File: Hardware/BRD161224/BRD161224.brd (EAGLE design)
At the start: 100 x 80 mm, 16 parts, among them Q1 DMP2035, Q2 FDV301, Q3 FDV301, Q4 DMP2035, Q5 DMP2035, Q6 DMP2035

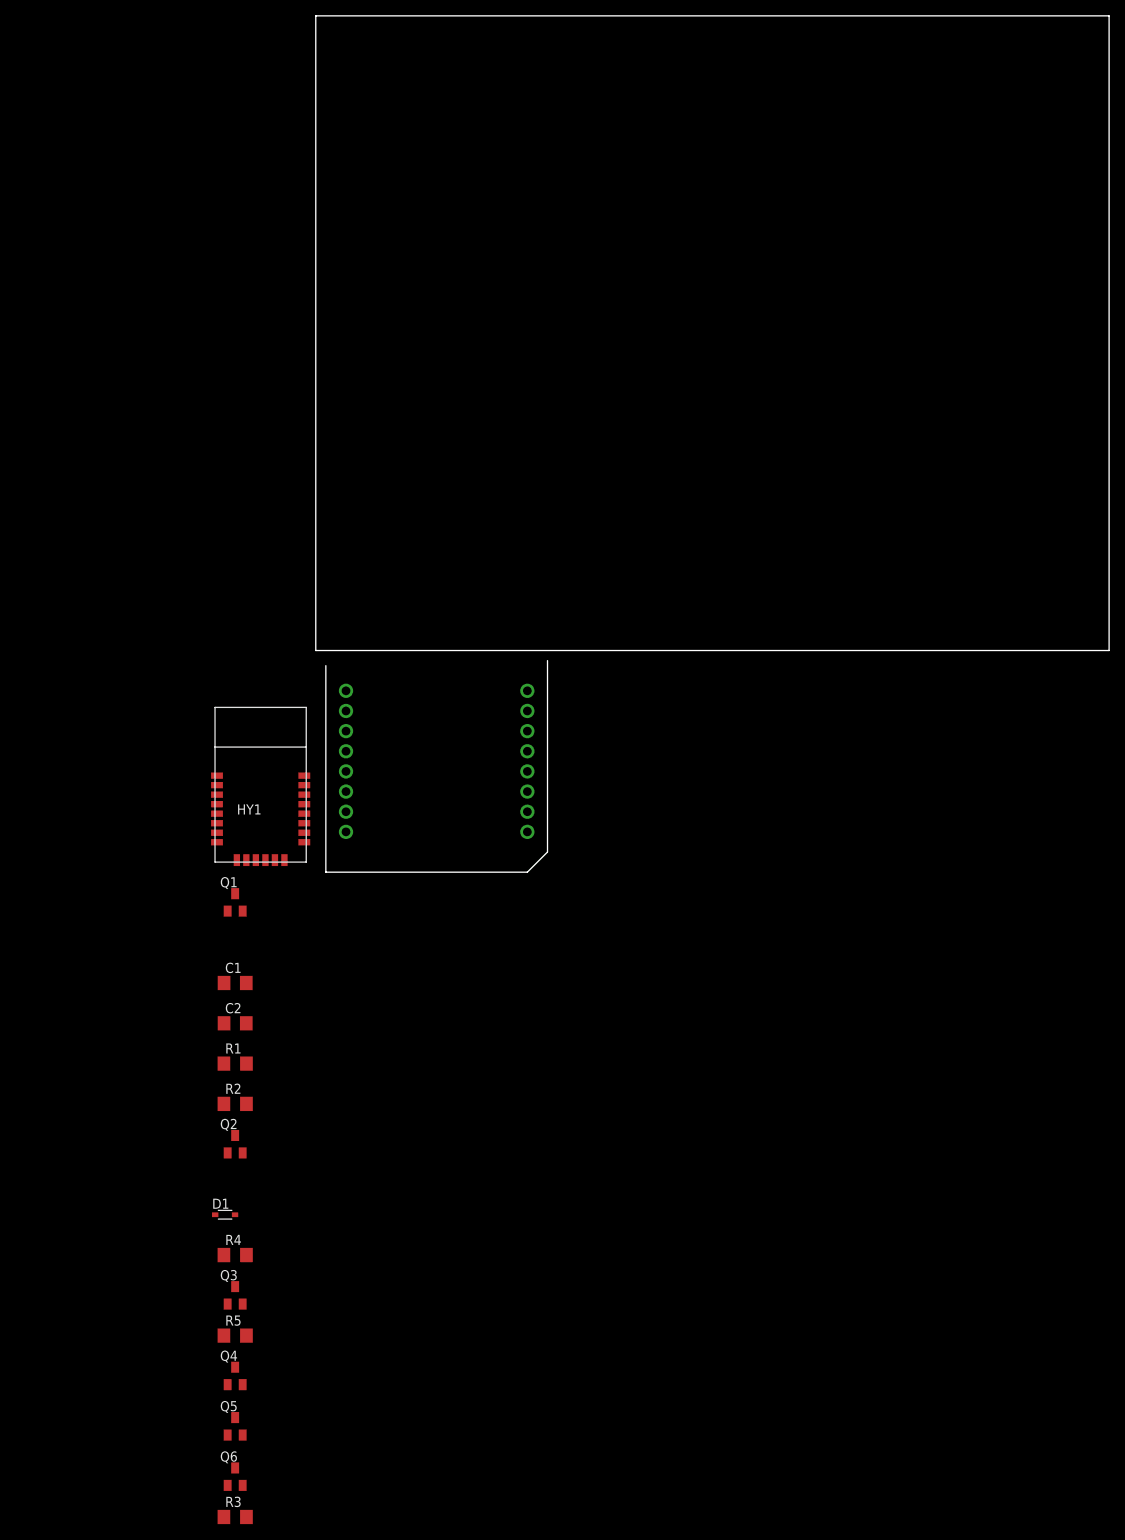
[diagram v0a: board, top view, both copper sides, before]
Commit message: ble2_click R00 finished
Signed-off-by: Christoph Tack <prog.send@gmail.com>
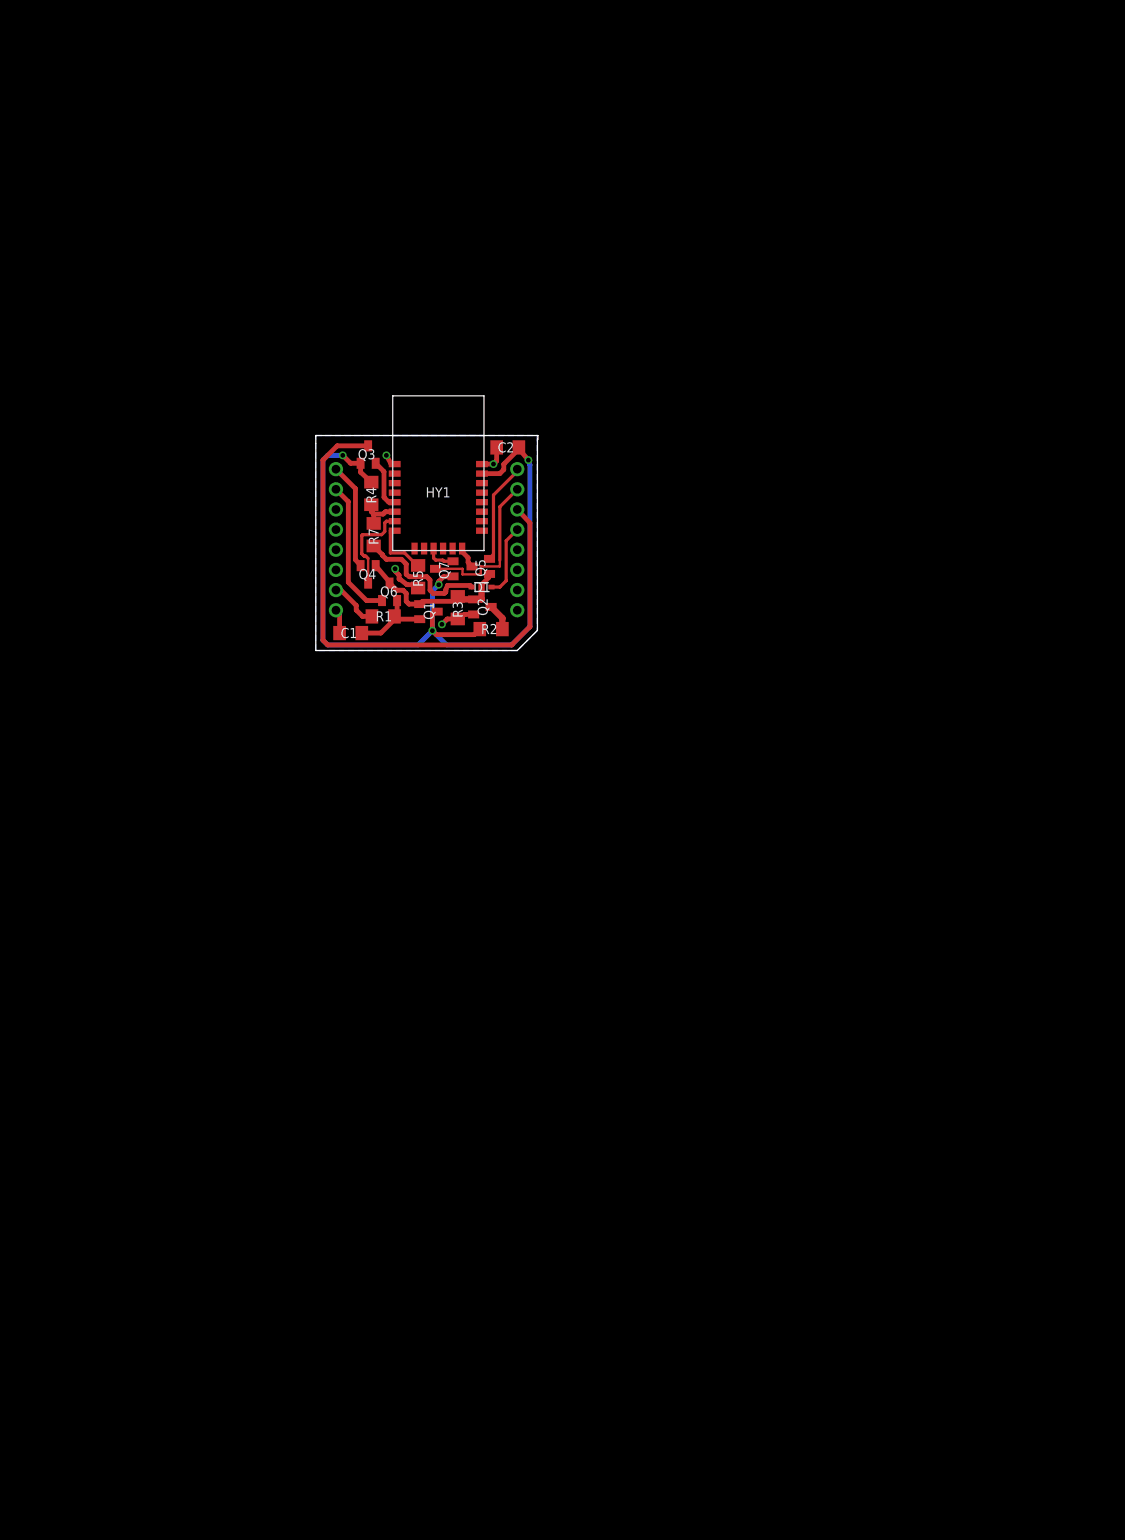
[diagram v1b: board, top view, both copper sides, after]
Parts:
- added DRILEGEND: (no value), drilegend:DRILEGEND
- added Q7: FDV301, lieBtrau:SC_SOT23
- added R7: 0E, lieBtrau:RE_1206
- added U$2: (no value), lieBtrau:MC_FRAME_A5
- moved R3 118.0 mm to (17.9, 5.40), turned to 90 degrees
- moved Q6 113.2 mm to (9.30, 7.40)
- moved Q5 112.7 mm to (20.8, 10.6), turned to 90 degrees
- moved Q3 107.3 mm to (6.60, 24.7)
- moved Q4 102.4 mm to (6.60, 9.60), turned to 180 degrees
- moved R5 98.4 mm to (12.9, 9.30), turned to 90 degrees
- moved R4 97.5 mm to (7.00, 19.8), turned to 90 degrees
- moved D1 85.5 mm to (20.9, 8.00), turned to 180 degrees
- moved C2 80.3 mm to (24.2, 25.6), turned to 180 degrees
- moved Q2 74.6 mm to (21.0, 5.50), turned to 270 degrees
- moved R2 68.0 mm to (22.1, 2.70), turned to 180 degrees
- moved R1 59.4 mm to (8.50, 4.30)
- moved C1 46.5 mm to (4.40, 2.20), turned to 180 degrees
- moved HY1 45.2 mm to (9.70, 12.6)
- moved Q1 44.0 mm to (14.2, 4.90), turned to 270 degrees
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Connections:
- new net N$16: HY1.6, R4.1, R7.2
- new net N$18: MC1.P$15, Q7.3
- net N$11: now also Q7.2; no longer MC1.P$15
- net N$2: now also Q7.1
- net N$8: now also R7.1; no longer HY1.6, R4.1
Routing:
- net N$2: track 0.00 -> 107.3 mm, vias 0 -> 4
- net N$10: track 0.00 -> 71.9 mm
- net N$4: track 0.00 -> 21.2 mm
- net N$18: track 0.00 -> 20.4 mm
- net N$6: track 0.00 -> 17.6 mm
- net GND: track 0.00 -> 17.3 mm, vias 0 -> 4
- net N$8: track 0.00 -> 17.2 mm
- net N$15: track 0.00 -> 13.4 mm
- net N$17: track 0.00 -> 12.7 mm
- net N$13: track 0.00 -> 12.0 mm
- net N$1: track 0.00 -> 10.7 mm
- net N$9: track 0.00 -> 9.20 mm
- net N$12: track 0.00 -> 8.21 mm
- net N$7: track 0.00 -> 6.33 mm
- net N$5: track 0.00 -> 6.25 mm
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- added copper zone on layer 16, net GND
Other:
- board size 100 x 80 mm -> 27.9 x 26.7 mm

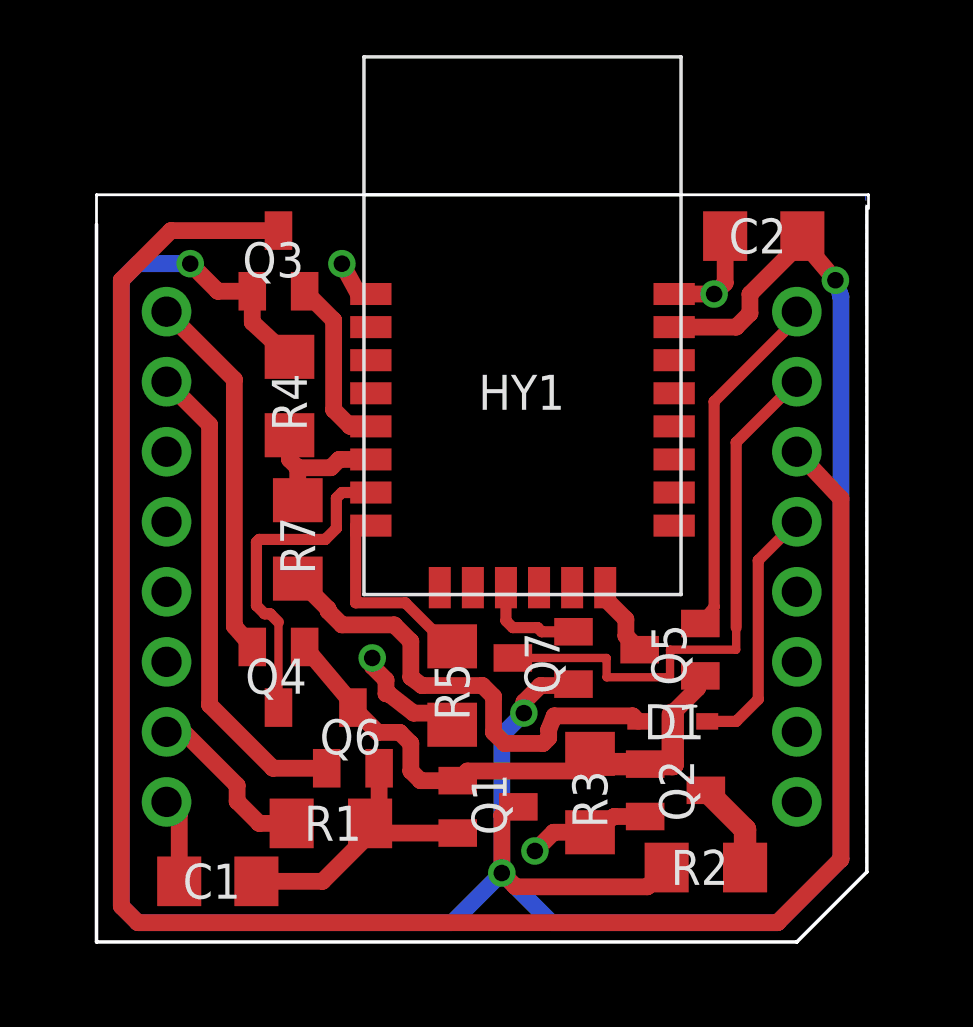
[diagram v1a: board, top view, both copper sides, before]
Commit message: Updating to Eagle 8.1.1 Adding two drill holes for easier mounting of pin headers Adding output files
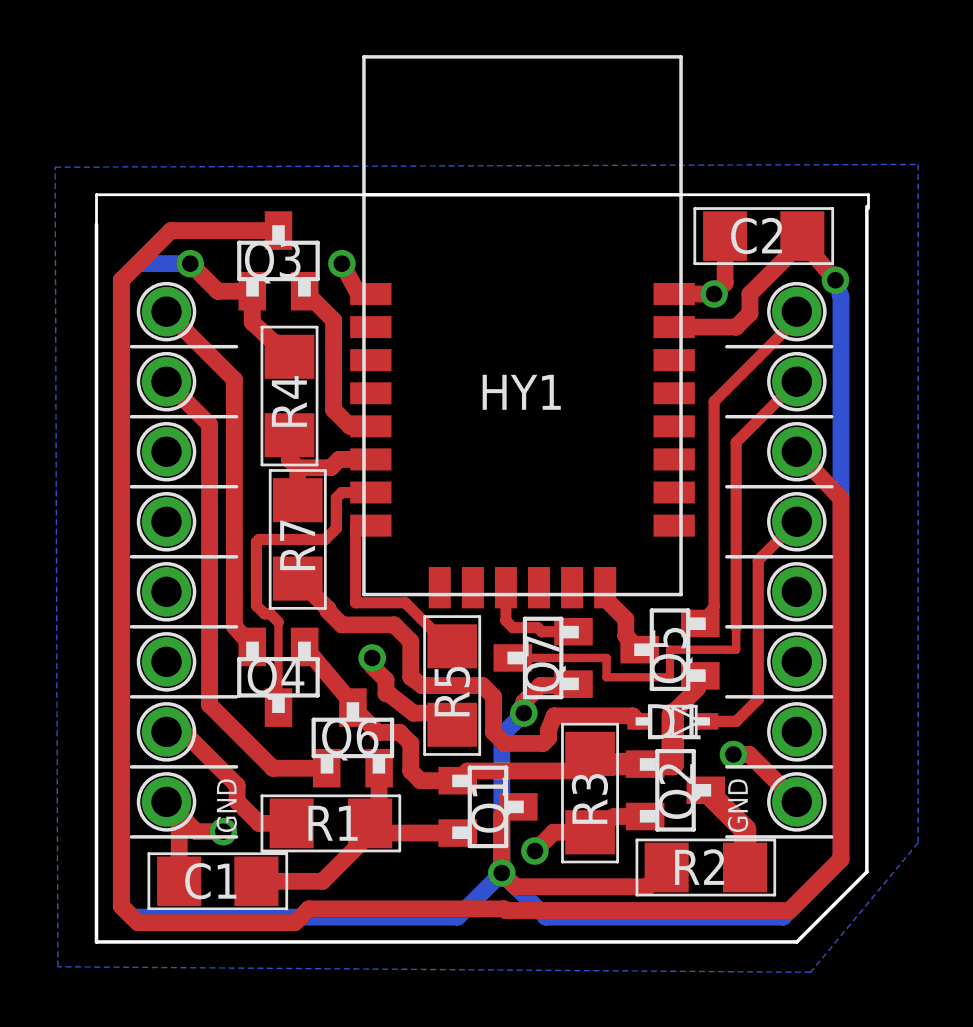
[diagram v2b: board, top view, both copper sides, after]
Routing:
- net GND: track 17.3 -> 22.8 mm, vias 4 -> 6
